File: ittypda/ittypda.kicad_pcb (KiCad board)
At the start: 2 copper layers, 149 parts, among them CN1 S2B-PH-SM4-TB, J1 USB_C_Receptacle_USB2.0_14P, J2 Conn_01x04_Pin, SW1 Switch, SW10 Switch, SW11 Switch, SW12 Switch, SW13 Switch, SW14 Switch, SW15 Switch, SW16 Switch, SW17 Switch, SW18 Switch, SW19 Switch, SW2 Switch, SW20 Switch, SW21 Switch, SW22 Switch, SW23 Switch, SW24 Switch, SW25 SLIDE SWITCH, SW26 Switch, SW27 Switch, SW28 Switch, SW29 Switch, SW3 Switch, SW30 Switch, SW31 Switch, SW32 Switch, SW33 Switch, SW34 Switch, SW36 Switch, SW37 Switch, SW38 Switch, SW39 Switch, SW4 Switch, SW41 Switch, SW42 Switch, SW43 Switch, SW44 Switch, SW45 Switch, SW46 Switch, SW47 Switch, SW48 Switch, SW49 Switch, SW5 Switch, SW50 Switch, SW51 Switch, SW52 Switch, SW53 Switch, SW54 Switch, SW55 Switch, SW56 Switch, SW57 Switch, SW58 Switch, SW59 Switch, SW6 Switch, SW60 Switch, SW61 Switch, SW7 Switch, SW8 Switch, SW9 Switch, U1 STM32F401RETx, U2 BQ24040DSQR, U3 TLV75801PDRV, Y1 16Mhz

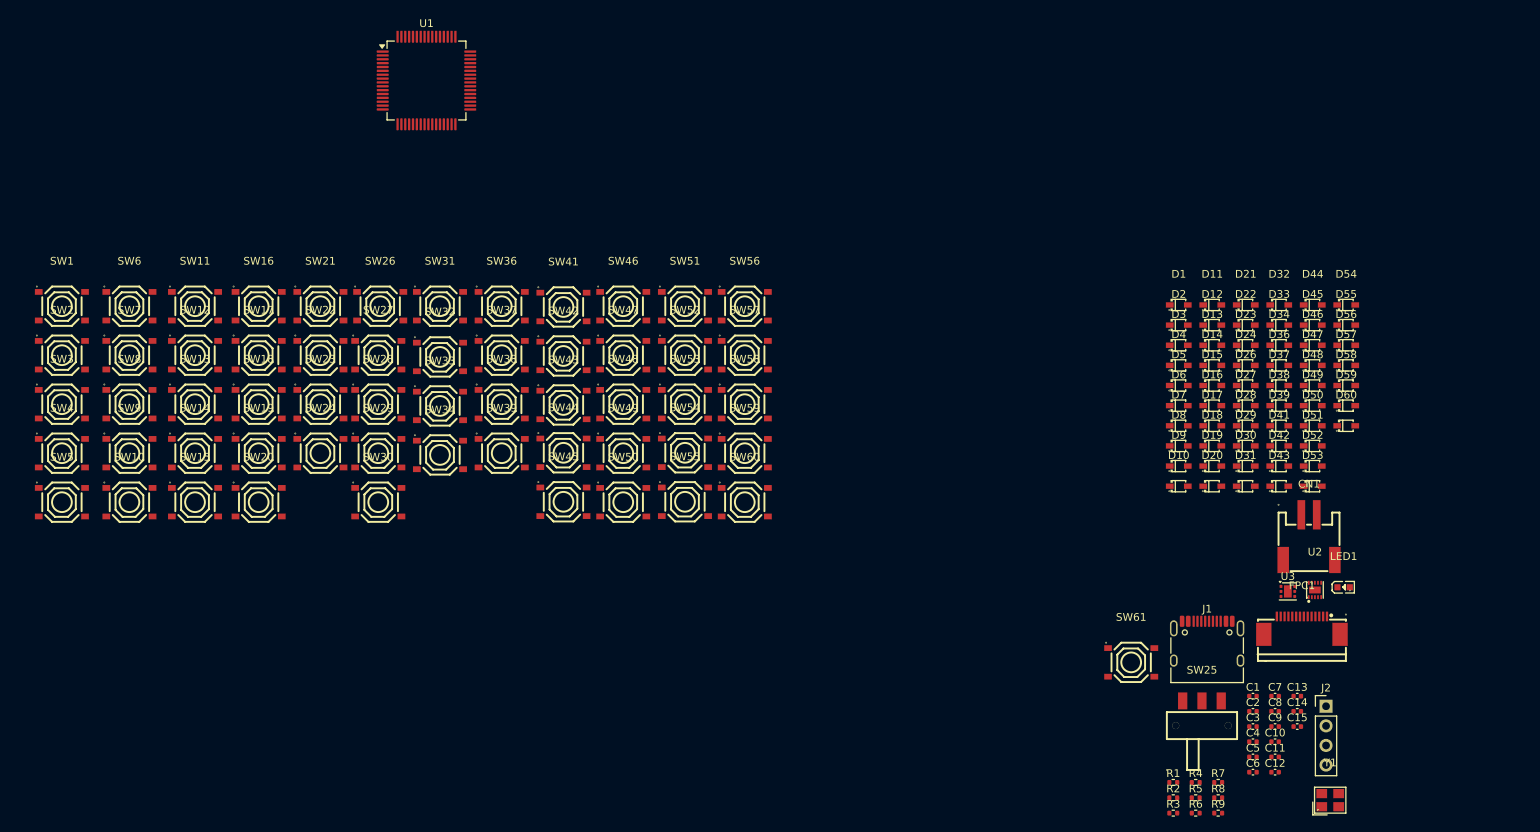
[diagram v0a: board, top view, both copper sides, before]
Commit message: place all caps and resistors (not final positions)
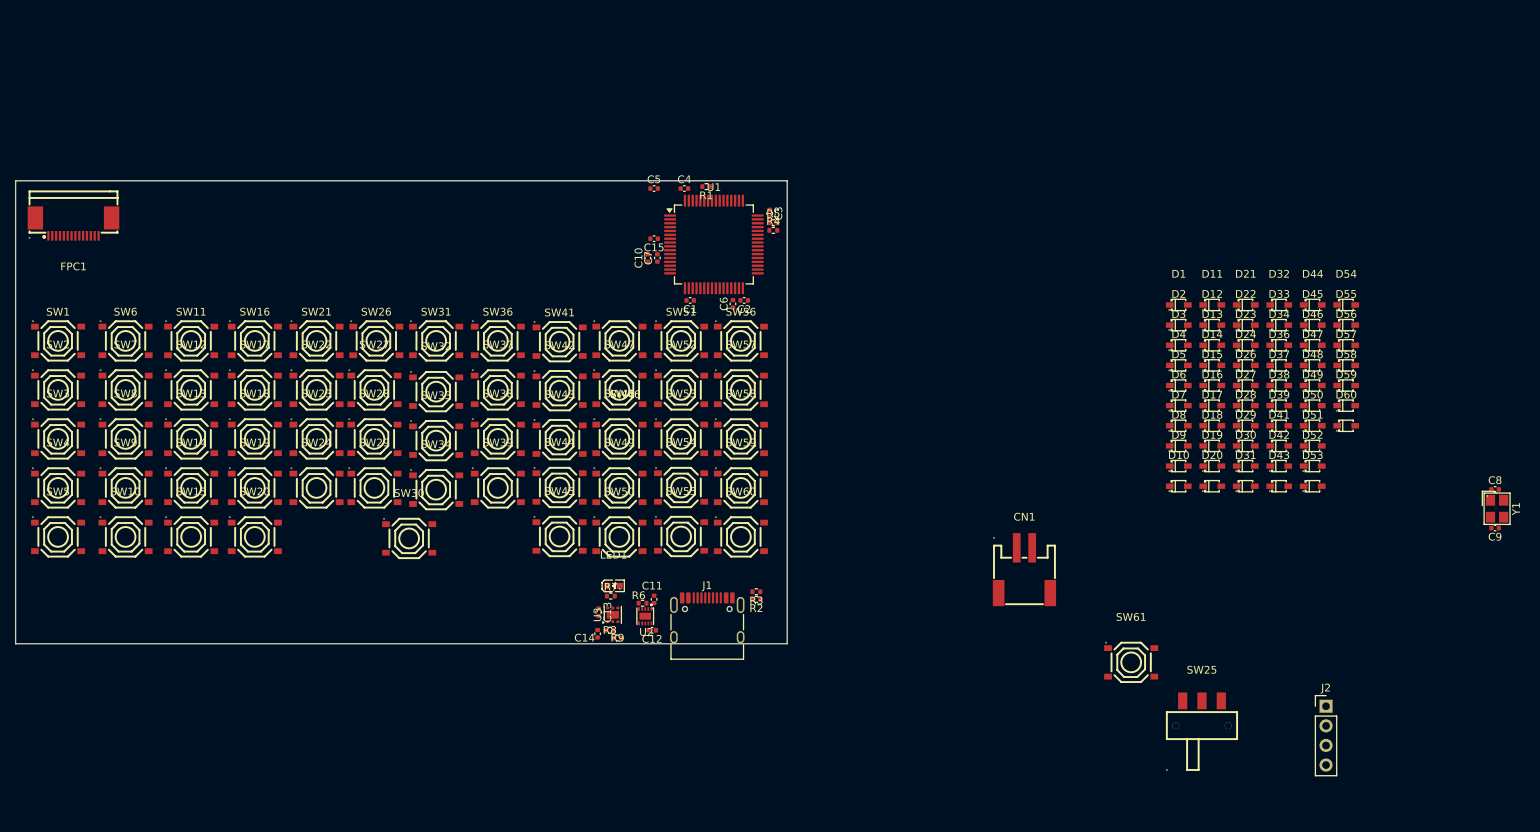
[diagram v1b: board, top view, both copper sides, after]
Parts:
- moved FPC1 167.4 mm to (35.8, 34.0), turned to 180 degrees
- moved C5 107.0 mm to (111.0, 29.0)
- moved C15 104.6 mm to (111.0, 35.5), turned to 180 degrees
- moved C4 102.8 mm to (114.9, 29.0)
- moved C10 102.7 mm to (110.2, 38.0), turned to 90 degrees
- moved C7 98.2 mm to (111.4, 38.0), turned to 90 degrees
- moved R1 98.1 mm to (117.8, 28.8), turned to 180 degrees
- moved LED1 94.6 mm to (105.8, 80.5)
- moved R5 92.5 mm to (126.5, 33.4)
- moved C3 91.4 mm to (126.0, 32.2), turned to -90 degrees
- moved C14 91.2 mm to (103.7, 86.7), turned to -90 degrees
- moved C13 91.2 mm to (103.8, 83.9), turned to -90 degrees
- moved C6 90.7 mm to (121.2, 43.9), turned to 90 degrees
- moved R4 90.1 mm to (126.5, 34.4)
- moved C1 89.2 mm to (115.7, 43.5), turned to 180 degrees
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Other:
- board outline added: 100 x 60 mm

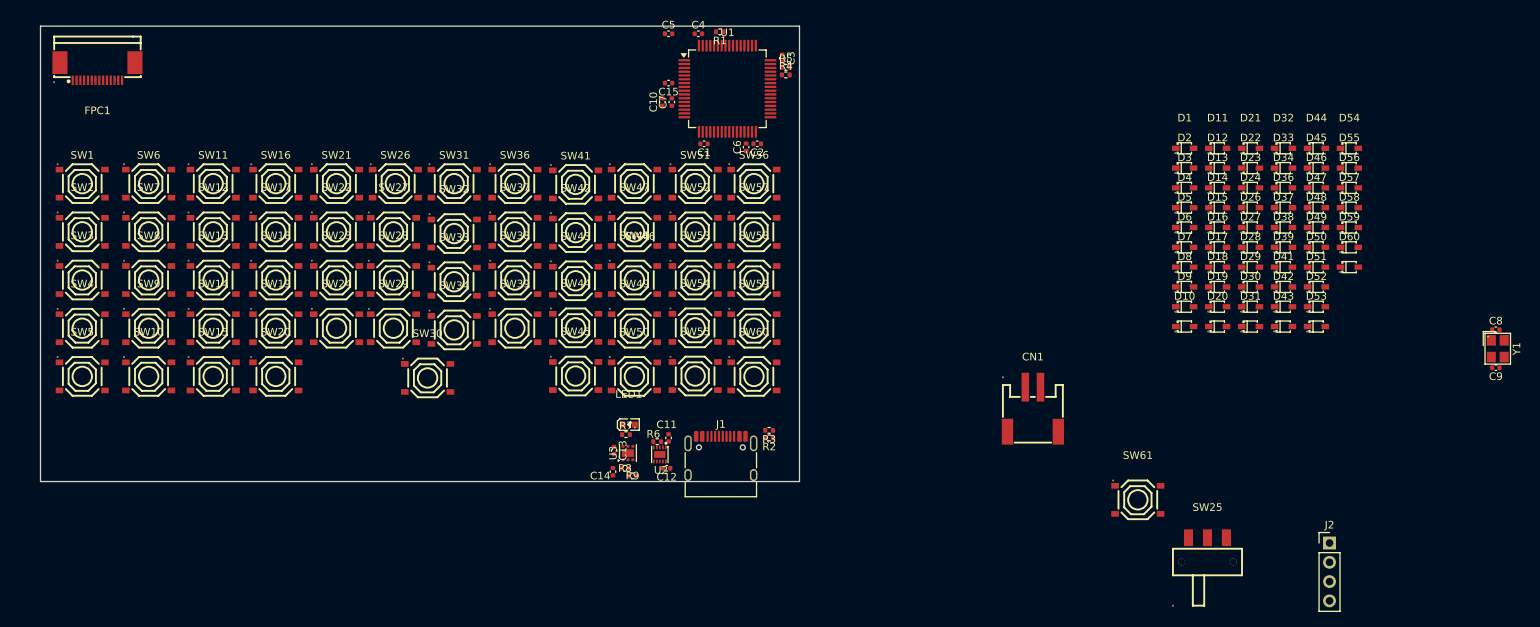
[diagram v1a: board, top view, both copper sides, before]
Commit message: add 3d model for usb c port and finalize initial placement of parts (not diodes yet)
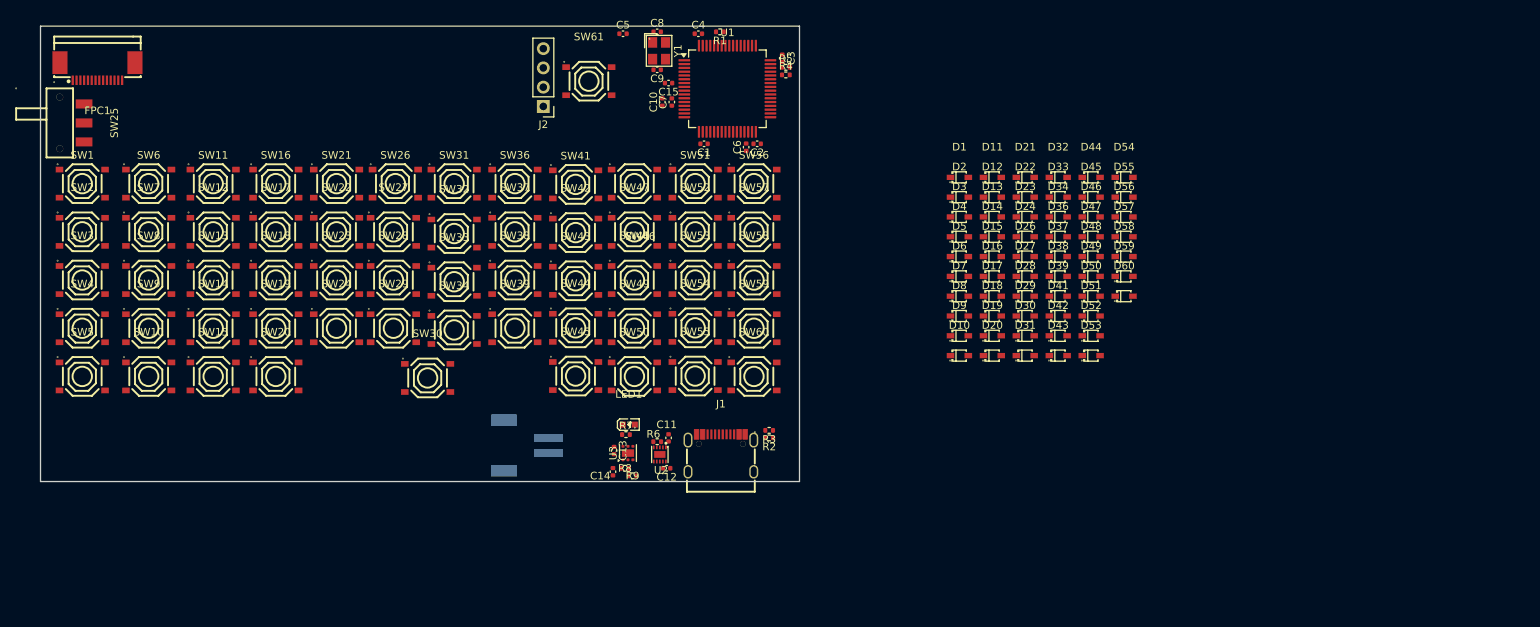
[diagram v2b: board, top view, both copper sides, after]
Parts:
- CN1: moved to B.Cu
- J1: footprint Connector_USB:USB_C_Receptacle_HRO_TYPE-C-31-M-12 -> easyeda2kicad:USB-C_SMD-TYPE-C-31-M-12_1
- moved SW25 157.8 mm to (34.0, 40.8), turned to -90 degrees
- moved J2 118.5 mm to (94.5, 38.6), turned to 180 degrees
- moved C8 117.3 mm to (109.5, 28.8)
- moved C9 117.3 mm to (109.5, 33.8)
- moved Y1 117.3 mm to (109.8, 31.2)
- moved SW61 91.0 mm to (100.5, 35.2)
- moved CN1 66.9 mm to (92.2, 83.2), turned to 90 degrees
- moved D1 29.9 mm to (149.3, 47.9)
- moved D10 29.9 mm to (149.3, 71.4)
- moved D11 29.9 mm to (153.7, 47.9)
- moved D12 29.9 mm to (153.7, 50.5)
- moved D13 29.9 mm to (153.7, 53.1)
- moved D14 29.9 mm to (153.7, 55.8)
- moved D15 29.9 mm to (153.7, 58.4)
- moved D16 29.9 mm to (153.7, 61.0)
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
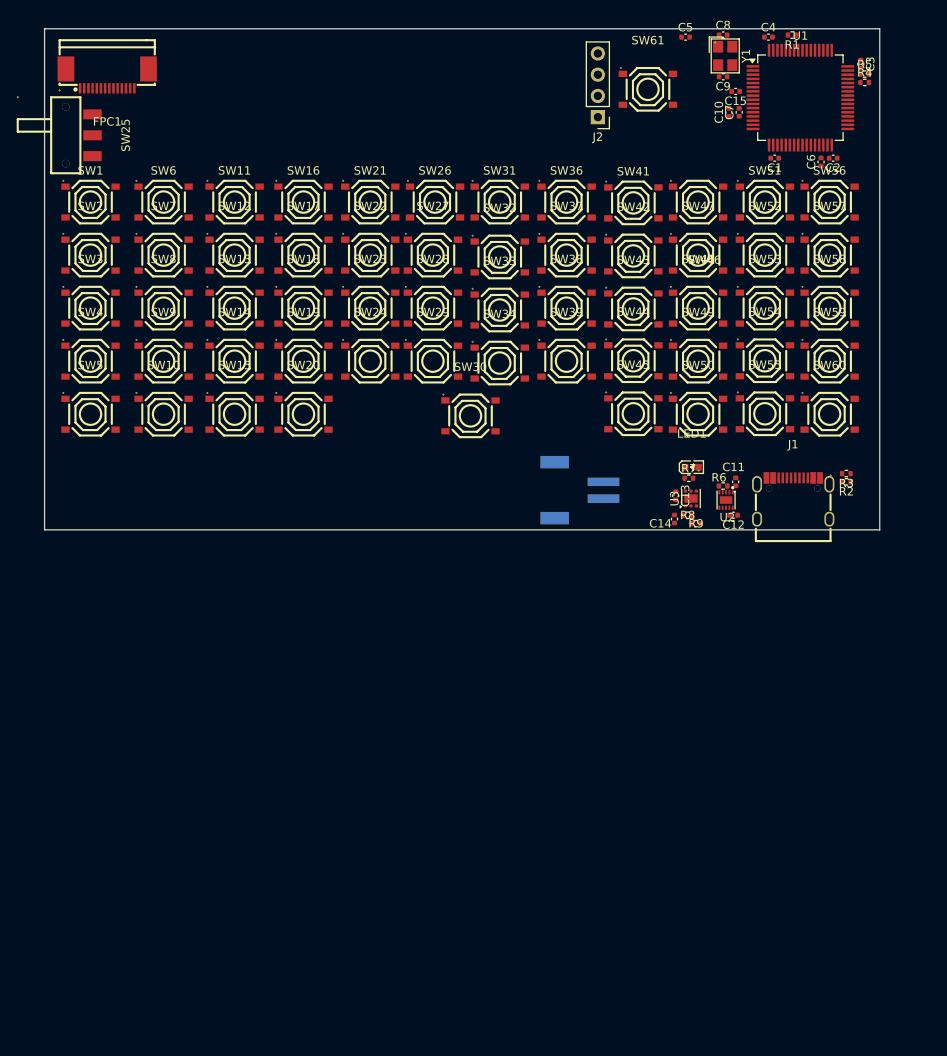
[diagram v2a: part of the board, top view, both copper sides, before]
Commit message: snap all keys to grid
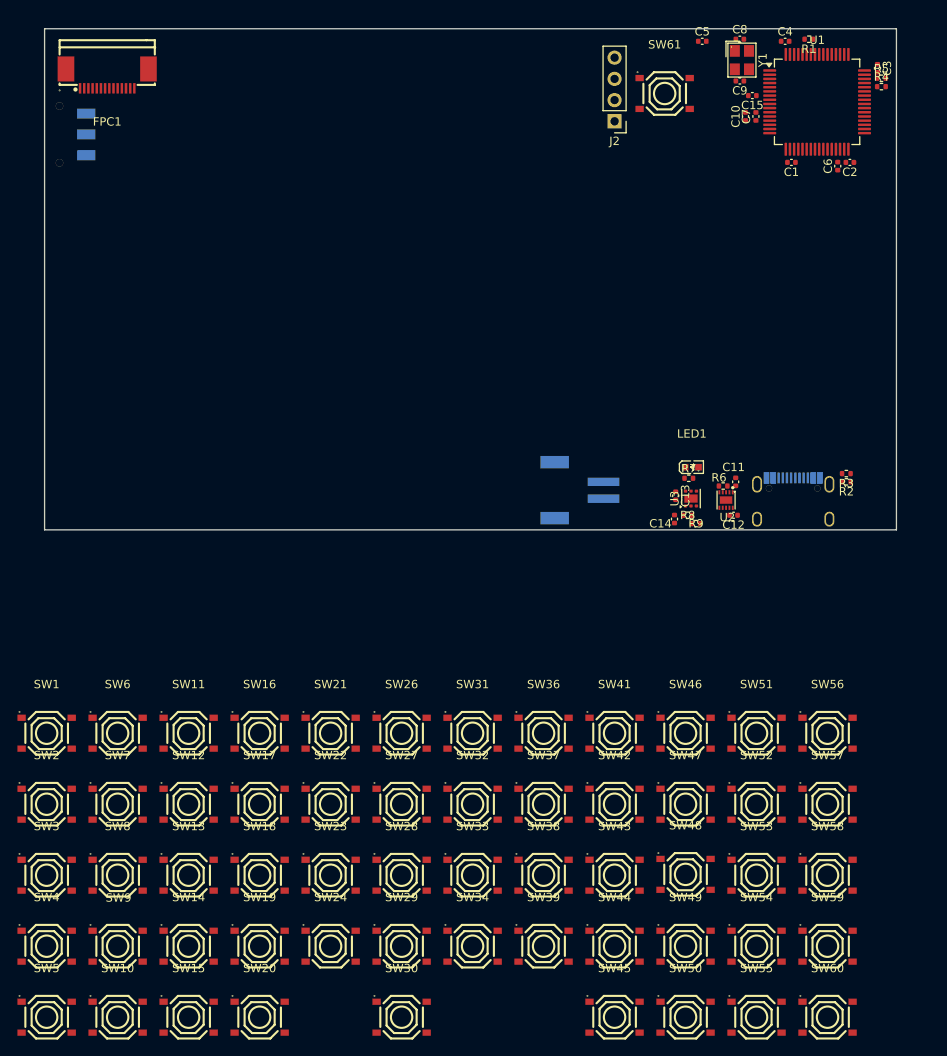
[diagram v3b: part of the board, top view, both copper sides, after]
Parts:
- J1, SW25: moved to B.Cu
- moved SW30 72.5 mm to (71.0, 146.3)
- moved SW10 72.4 mm to (37.0, 146.3)
- moved SW15 72.4 mm to (45.5, 146.3)
- moved SW20 72.4 mm to (54.0, 146.3)
- moved SW5 72.4 mm to (28.5, 146.3)
- moved SW45 72.3 mm to (96.5, 146.3)
- moved SW55 72.3 mm to (113.5, 146.3)
- moved SW50 72.2 mm to (105.0, 146.3)
- moved SW60 72.2 mm to (122.0, 146.3)
- moved SW14 70.3 mm to (45.5, 137.8)
- moved SW9 70.3 mm to (37.0, 137.8)
- moved SW19 70.2 mm to (54.0, 137.8)
- moved SW4 70.2 mm to (28.5, 137.8)
- moved SW24 70.2 mm to (62.5, 137.8)
- moved SW29 70.2 mm to (71.0, 137.8)
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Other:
- board size 100 x 60 mm -> 102 x 60 mm

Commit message: placed all switch diodes!
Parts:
- moved SW25 203.3 mm to (236.5, 42.0)
- moved D5 146.5 mm to (34.0, 148.8), turned to 90 degrees
- moved C11 145.1 mm to (253.8, 56.2)
- moved C12 145.1 mm to (253.5, 60.2)
- moved C13 145.1 mm to (246.6, 57.9)
- moved C14 145.1 mm to (246.4, 60.7)
- moved CN1 145.1 mm to (235.0, 57.2)
- moved J1 145.1 mm to (260.6, 58.2)
- moved LED1 145.1 mm to (248.5, 54.5)
- moved R2 145.1 mm to (267.0, 56.2)
- moved R3 145.1 mm to (267.0, 55.3)
- moved R6 145.1 mm to (252.2, 56.8)
- moved R7 145.1 mm to (248.1, 55.8)
- moved R8 145.1 mm to (248.0, 60.2)
- moved R9 145.1 mm to (249.0, 61.2)
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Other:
- board size 102 x 60 mm -> 102 x 66 mm

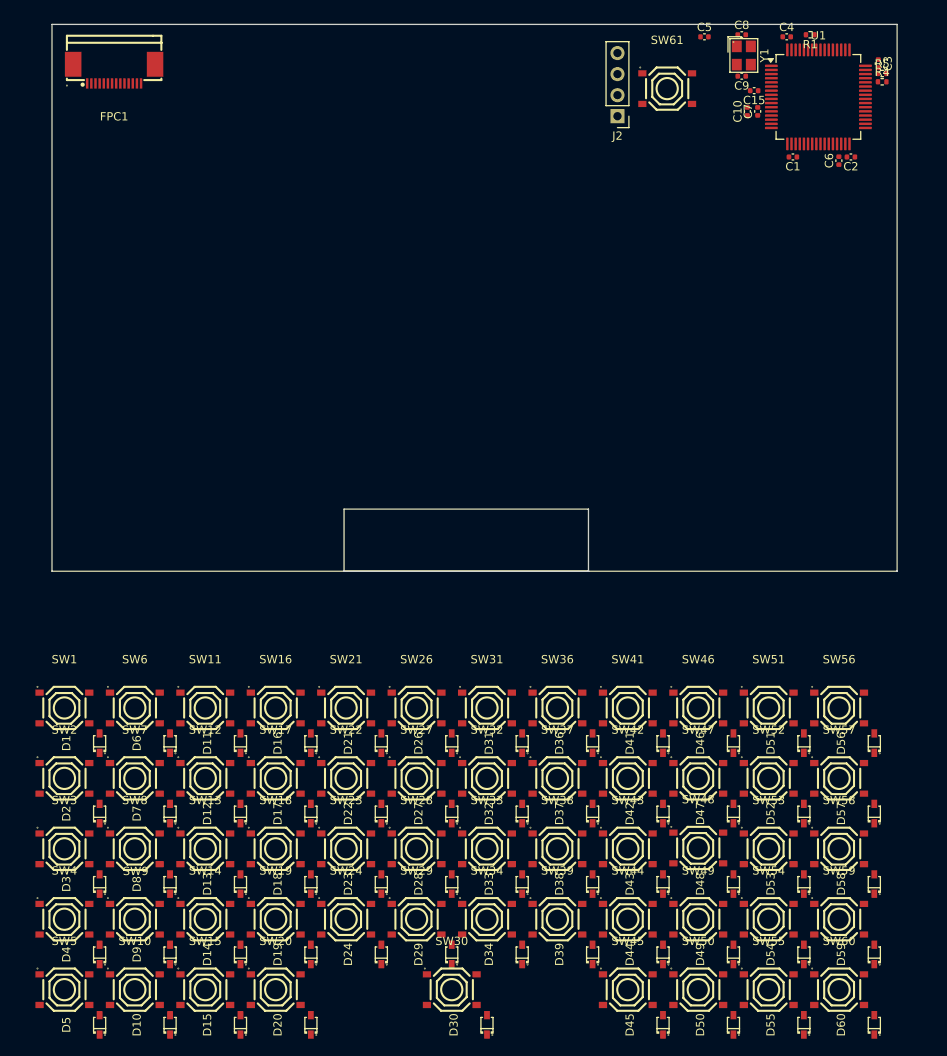
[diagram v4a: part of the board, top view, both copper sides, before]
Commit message: layout front side of board
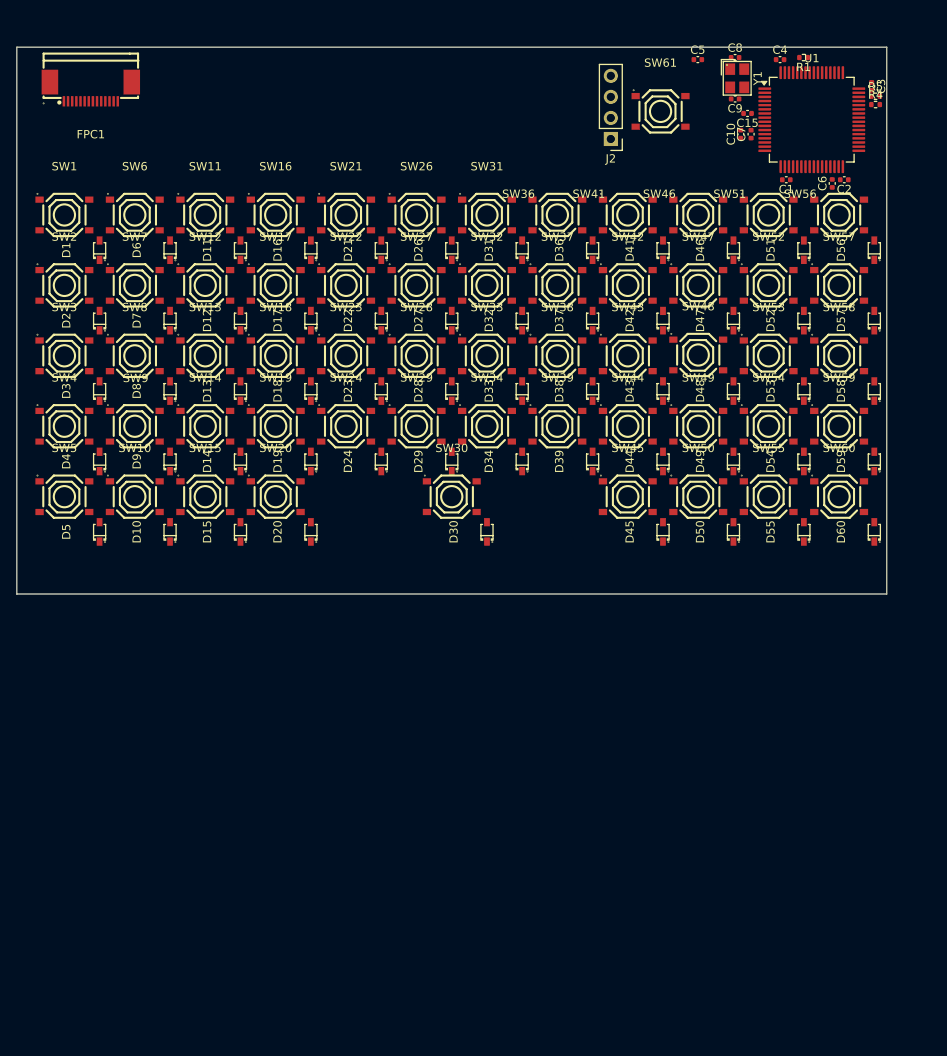
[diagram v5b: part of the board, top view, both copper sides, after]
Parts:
- moved D1 59.5 mm to (34.0, 55.2)
- moved D10 59.5 mm to (42.5, 89.2)
- moved D11 59.5 mm to (51.0, 55.2)
- moved D12 59.5 mm to (51.0, 63.8)
- moved D13 59.5 mm to (51.0, 72.2)
- moved D14 59.5 mm to (51.0, 80.8)
- moved D15 59.5 mm to (51.0, 89.2)
- moved D16 59.5 mm to (59.5, 55.2)
- moved D17 59.5 mm to (59.5, 63.8)
- moved D18 59.5 mm to (59.5, 72.2)
- moved D19 59.5 mm to (59.5, 80.8)
- moved D2 59.5 mm to (34.0, 63.8)
- moved D20 59.5 mm to (59.5, 89.2)
- moved D21 59.5 mm to (68.0, 55.2)
- moved D22 59.5 mm to (68.0, 63.8)
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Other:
- board size 102 x 66 mm -> 105 x 66 mm
